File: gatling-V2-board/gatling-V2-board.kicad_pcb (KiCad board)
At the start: 2 copper layers, 65 x 45 mm, 33 parts, among them IC2 TRANSCEIVER_CAN_33, J1 645002114822, J10 61900311121, J11 61900311121, J12 61900311121, J13 61900311121, J2 62000411622, J3 61900311121, J4 61900311121, J5 691311700102, J7 653006114822, J9 62000411622, U1 Teensy3.2

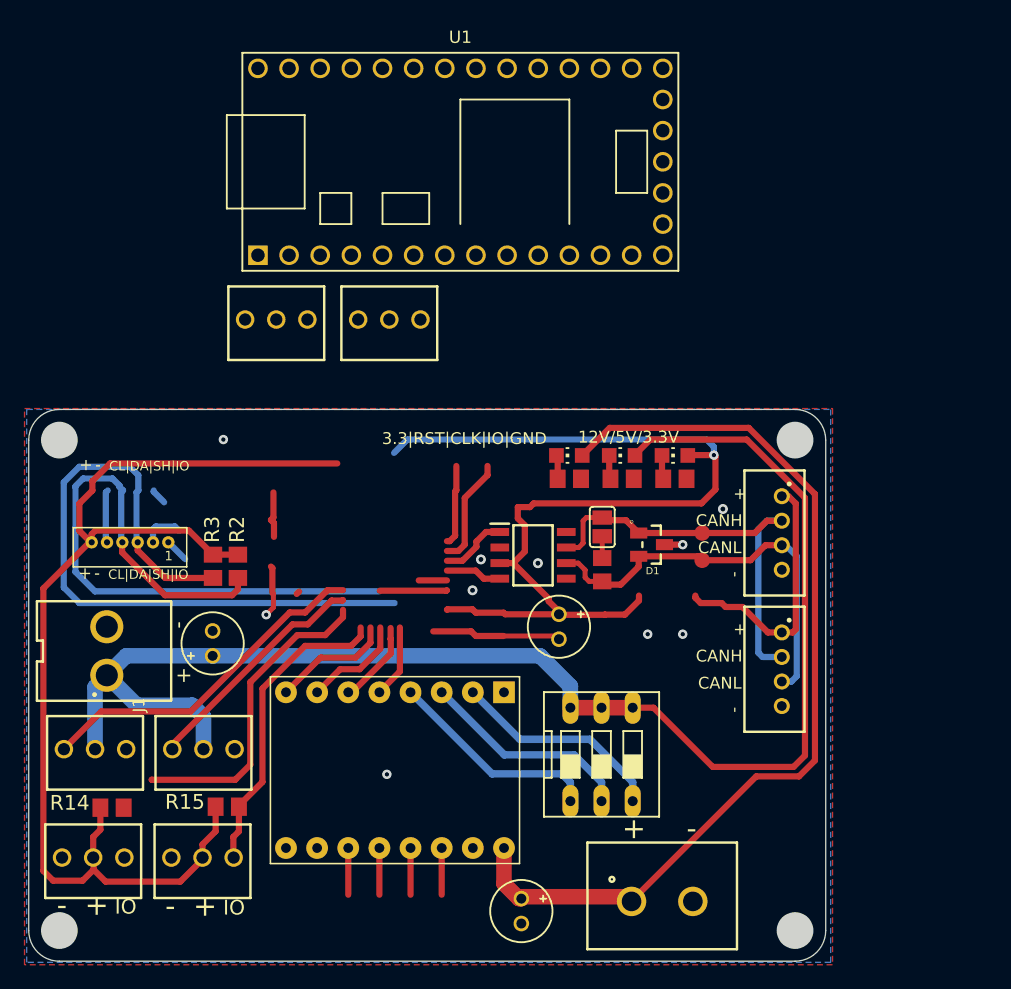
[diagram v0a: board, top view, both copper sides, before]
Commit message: Lib composant créée+pcb gatling mises à jours avec teensy (a verifier avant prod)
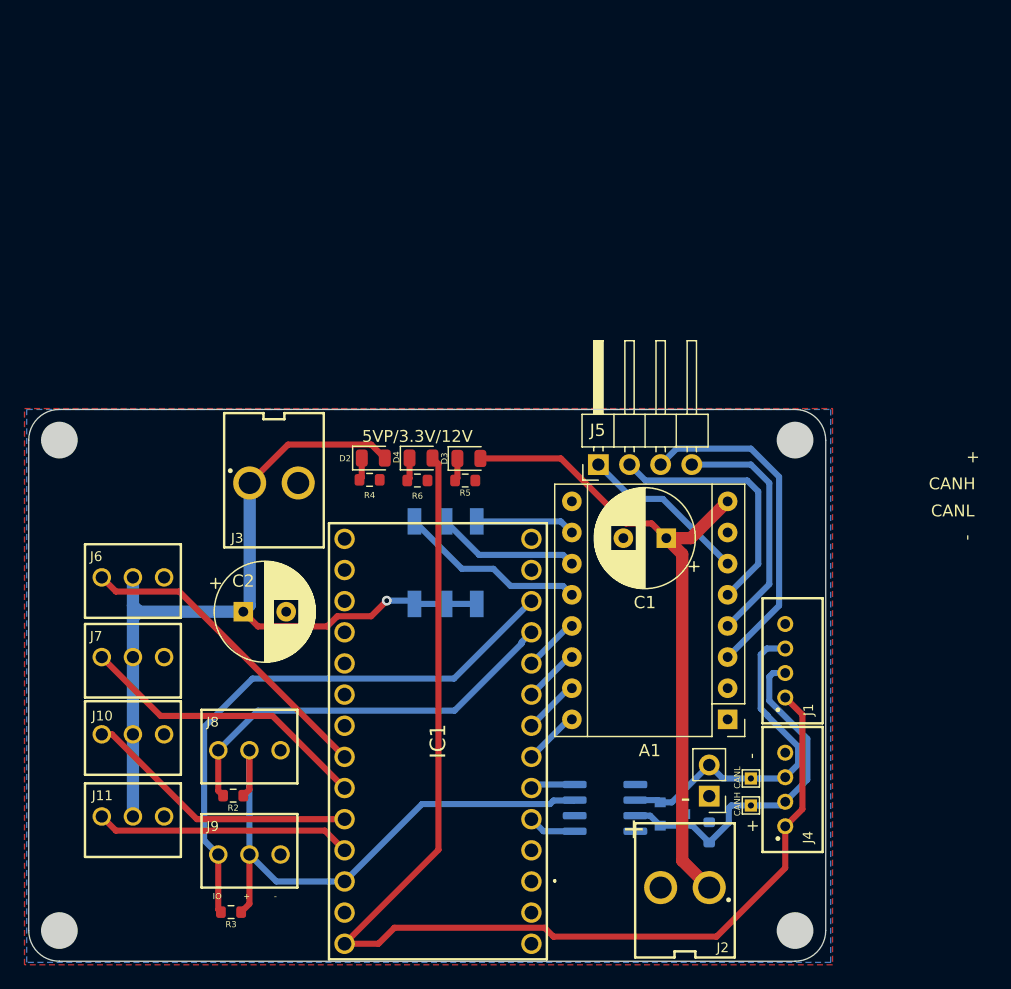
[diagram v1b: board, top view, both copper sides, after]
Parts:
- removed IC2: TRANSCEIVER_CAN_33, schematic prebarillet:SOIC127P600X175-8N
- removed J12, J13: 61900311121, schematic prebarillet:61900311121
- removed LED1, LED2, LED3: LED0805CHIP-LED0805, schematic prebarillet:CHIP-LED0805
- removed R12, R13: R0805R0805, schematic prebarillet:R0805
- removed R14, R15: R-EU_R0805, schematic prebarillet:R0805
- removed R7: 120, schematic prebarillet:R0805
- removed S1: DS03, schematic prebarillet:DS-03
- removed SJ1: SJ, schematic prebarillet:SJ
- removed U$1: DRV8825, schematic prebarillet:DRV8825
- removed U$2, U$3, U$4: 100uF, schematic prebarillet:E2-5
- added A1: Pololu_Breakout_DRV8825, Module:Pololu_Breakout-16_15.2x20.3mm, F.Cu at (173.0, 107.8)
- added C1: 100µF, Capacitor_THT:CP_Radial_D8.0mm_P3.50mm, F.Cu at (168.0, 93.0)
- added C2: 100µF, Capacitor_THT:CP_Radial_D8.0mm_P3.50mm, F.Cu at (133.5, 99.0)
- added D2: LED, LED_SMD:LED_0805_2012Metric, F.Cu at (144.1, 86.5)
- added D3: LED, LED_SMD:LED_0805_2012Metric, F.Cu at (151.9, 86.5)
- added D4: LED, LED_SMD:LED_0805_2012Metric, F.Cu at (148.0, 86.5)
- added IC1: TEENSY3.2, AREA_lib_composant:TEENSY32, F.Cu at (157.0, 121.0)
- added J6: Conn_01x03_Male, AREA_lib_Connector:Wuerth_2.54mm_3pins_61900311121, F.Cu at (124.5, 96.5)
- added J8: Conn_01x03_Male, AREA_lib_Connector:Wuerth_2.54mm_3pins_61900311121, F.Cu at (134.0, 110.0)
- added JP1: Jumper, Connector_PinHeader_2.54mm:PinHeader_1x02_P2.54mm_Vertical, F.Cu at (171.5, 114.0)
- added R4: 520, Resistor_SMD:R_0603_1608Metric, F.Cu at (143.8, 88.2)
- added R5: 520, Resistor_SMD:R_0603_1608Metric, F.Cu at (151.6, 88.3)
- added R6: 520, Resistor_SMD:R_0603_1608Metric, F.Cu at (147.7, 88.3)
- added SW1: SW_DIP_x03, Button_Switch_SMD:SW_DIP_SPSTx03_Slide_6.7x9.18mm_W6.73mm_P2.54mm_LowProfile_JPin, B.Cu at (150.0, 95.0)
- D1: value 5Vdc -> D_TVS_x2_AAC; footprint schematic prebarillet:WE-TVS_SOT23-3L -> Package_TO_SOT_SMD:SOT-23; moved to B.Cu
- J1: value 645002114822 -> Conn_01x04_Male; footprint schematic prebarillet:645002114822 -> AREA_lib_Connector:Wuerth_2mm_4pin_62000411622
- J10, J11: value 61900311121 -> Conn_01x03_Male; footprint schematic prebarillet:61900311121 -> AREA_lib_Connector:Wuerth_2.54mm_3pins_61900311121
- J2: value 62000411622 -> Conn_01x02_Male; footprint schematic prebarillet:62000411622 -> AREA_lib_Connector:Wuerth_3.96mm_2pin_645002114822
- J3: value 61900311121 -> Conn_01x02_Male; footprint schematic prebarillet:61900311121 -> AREA_lib_Connector:Wuerth_3.96mm_2pin_645002114822
- J4: value 61900311121 -> Conn_01x04_Male; footprint schematic prebarillet:61900311121 -> AREA_lib_Connector:Wuerth_2mm_4pin_62000411622
- J5: value 691311700102 -> Conn_01x04_Male; footprint schematic prebarillet:691311700102 -> Connector_PinHeader_2.54mm:PinHeader_1x04_P2.54mm_Horizontal
- J7: value 653006114822 -> Conn_01x03_Male; footprint schematic prebarillet:653006114822 -> AREA_lib_Connector:Wuerth_2.54mm_3pins_61900311121
- J9: value 62000411622 -> Conn_01x03_Male; footprint schematic prebarillet:62000411622 -> AREA_lib_Connector:Wuerth_2.54mm_3pins_61900311121
- R1: value R0805R0805 -> 120; footprint schematic prebarillet:R0805 -> Resistor_SMD:R_0603_1608Metric; moved to B.Cu
- R2, R3: value R-EU_R0805 -> 10K; footprint schematic prebarillet:R0805 -> Resistor_SMD:R_0603_1608Metric
- TP1, TP2: value TEST-POINT3X5 -> TestPoint; footprint schematic prebarillet:PAD.03X.05 -> TestPoint:TestPoint_THTPad_1.0x1.0mm_Drill0.5mm
- U1: value Teensy3.2 -> SN65HVD232; footprint teensy:Teensy30_31_32_LC -> Package_SO:SOIC-8_3.9x4.9mm_P1.27mm; moved to B.Cu
- moved J1 56.4 mm to (178.3, 103.0)
- moved U1 54.0 mm to (163.0, 115.0)
- moved J4 50.3 mm to (178.3, 113.5), turned to 270 degrees
- moved J9 45.3 mm to (134.0, 118.5), turned to 180 degrees
- moved J5 36.0 mm to (162.5, 87.0), turned to 90 degrees
- moved R1 31.0 mm to (171.5, 117.0), turned to 270 degrees
- moved J2 30.3 mm to (169.5, 122.0), turned to 0 degrees
- moved R3 28.2 mm to (132.5, 123.5), turned to 180 degrees
- moved TP1 22.6 mm to (174.9, 114.8), turned to 90 degrees
- moved D1 22.0 mm to (168.5, 115.5), turned to 0 degrees
- moved R2 18.7 mm to (132.7, 114.0), turned to 180 degrees
- moved TP2 18.2 mm to (174.9, 112.6), turned to 90 degrees
- moved J3 12.5 mm to (136.0, 88.0), turned to 180 degrees
- moved J7 9.66 mm to (124.5, 103.0)
- moved J11 7.95 mm to (124.5, 116.0)
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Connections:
- D1 pad 1: /CANH -> CANH
- D1 pad 2: /CANL -> CANL
- J1 pad 2: GND -> CANH
- J10 pad 2: +5V -> +5VP
- J10 pad 3: /SERVO1 -> SERVO3
- J11 pad 2: +5V -> +5VP
- J11 pad 3: /SERVO2 -> SERVO4
- J2 pad 1: /5VC -> +12V
- J2 pad 2: /CANH -> GND
- J3 pad 1: GND -> +5VP
- J3 pad 2: +5V -> GND
- J4 pad 1: GND -> +5V
- J4 pad 2: +5V -> CANH
- J4 pad 3: /SERVO4 -> CANL
- J5 pad 1: /+12V -> Net-(A1-Pad6)
- J5 pad 2: GND -> Net-(A1-Pad5)
- J7 pad 1: /GPIO1 -> GND
- J7 pad 2: /XSHUT1 -> +5VP
- J7 pad 3: /SDA -> SERVO2
- J9 pad 1: /5VC -> FOURCHE2
- J9 pad 2: /CANH -> +3V3
- J9 pad 3: /CANL -> GND
- R1 pad 1: GND -> Net-(JP1-Pad1)
- R1 pad 2: Net-(LED3-PadC) -> CANH
- R2 pad 1: /SCL -> +3V3
- R2 pad 2: /+3.3V -> FOURCHE1
- R3 pad 1: /SDA -> +3V3
- R3 pad 2: /+3.3V -> FOURCHE2
- U1 pad 1: GND -> CAN_TX
- U1 pad 2: Net-(U1-Pad2) -> GND
- U1 pad 3: Net-(U1-Pad3) -> +3V3
- U1 pad 4: /DIR -> CAN_RX
- U1 pad 5: /CANTX -> (no net)
- U1 pad 6: /CANRX -> CANL
- U1 pad 7: /SLIP -> CANH
- U1 pad 8: /STEP -> (no net)
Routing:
- net /+3.3V: track 171.4 -> 0.00 mm, vias 1 -> 0
- net /+12V: track 77.7 -> 0.00 mm
- net +5VP: track 0.00 -> 73.4 mm, vias 0 -> 1
- net /SCL: track 59.7 -> 0.00 mm
- net /SDA: track 58.8 -> 0.00 mm
- net +12V: track 0.00 -> 54.0 mm
- net +3V3: track 0.00 -> 47.6 mm
- net FOURCHE2: track 0.00 -> 46.6 mm
- net /CANH: track 34.9 -> 0.00 mm
- net /CANL: track 33.5 -> 0.00 mm
- net FOURCHE1: track 0.00 -> 33.5 mm
- net CANH: track 0.00 -> 28.9 mm
- net /SERVO1: track 28.1 -> 0.00 mm
- net CANL: track 0.00 -> 28.0 mm
- net Net-(A1-Pad3): track 0.00 -> 27.6 mm
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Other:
- net class Default: clearance 0.2 -> 0.15
- rule trace_clearance: 0.2 -> 0.15
- board text added: "5VP/3.3V/12V"
- board text added: "Carte pre-barillet /*A.R.E.A.OLD*/ V2 PA-github.com/kingovchouffe"
- board text removed: "12V/5V/3.3V"
- board text removed: "3.3|RST|CLK|IO|GND"
- board text removed: "CL|DA|SH|IO"
- board text removed: "Carte pre-barillet /*A.R.E.A.OLD*/ V1 PA-github.com/kingovchouffe"

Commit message: prete pour inspection
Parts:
- SW1: moved to F.Cu
- moved C1 0.40 mm to (168.4, 93.0)
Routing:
- net Net-(A1-Pad10): track 8.13 -> 15.8 mm, vias 0 -> 1
- net +5V: track 97.1 -> 103.4 mm
- net Net-(A1-Pad12): track 15.3 -> 12.4 mm, vias 0 -> 1
- net Net-(A1-Pad11): track 11.7 -> 12.8 mm, vias 0 -> 1
- net SERVO3: track 22.7 -> 23.3 mm
- net +5VP: track 73.4 -> 73.7 mm, vias 1 -> 0
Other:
- board text added: "12V"
- board text added: "5V"
- board text added: "SERVO1"
- board text added: "SERVO2"
- board text added: "SERVO3"
- board text added: "SERVO4"

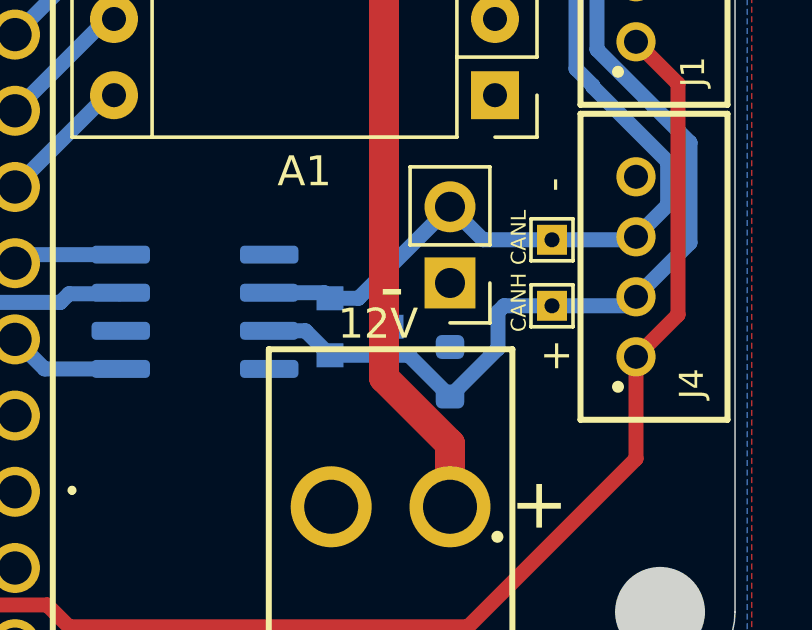
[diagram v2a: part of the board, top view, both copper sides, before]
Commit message: connect wire that weren't connected
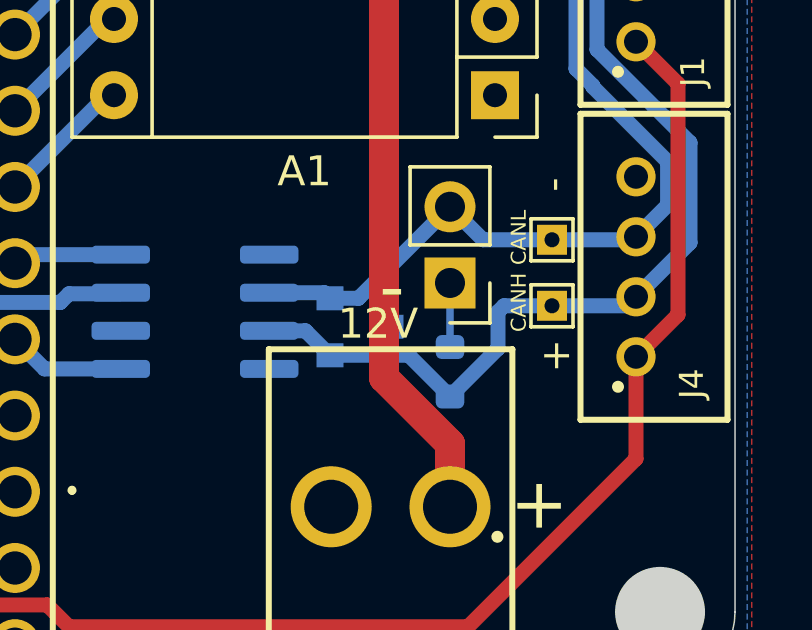
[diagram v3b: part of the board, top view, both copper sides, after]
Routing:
- net Net-(JP1-Pad1): track 0.00 -> 2.13 mm
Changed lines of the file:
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@@
-(kicad_pcb (version 20171130) (host pcbnew "(5.1.8)-1")
+(kicad_pcb (version 20171130) (host pcbnew "(5.1.6)-1")
   (general
     (thickness 1.6)
     (drawings 35)
-    (tracks 182)
+    (tracks 183)
     (zones 0)
     (modules 30)
@@
   )
   (setup
-    (last_trace_width 0.5)
+    (last_trace_width 0.25)
     (user_trace_width 0.5)
     (user_trace_width 0.75)
@@
   (segment (start 157.985 116.905) (end 160.525 116.905) (width 0.5) (layer B.Cu) (net 29))
   (segment (start 157 115.92) (end 157.985 116.905) (width 0.5) (layer B.Cu) (net 29))
+  (segment (start 171.5 116.175) (end 171.5 114.04) (width 0.25) (layer B.Cu) (net 30))
   (zone (net 1) (net_name GND) (layer B.Cu) (hatch edge 0.508)
     (priority 6)
     (connect_pads (clearance 0.000001))
     (min_thickness 0.0762)
-    (fill (arc_segments 32) (thermal_gap 0.2024) (thermal_bridge_width 0.2024))
+    (fill yes (arc_segments 32) (thermal_gap 0.2024) (thermal_bridge_width 0.2024))
     (polygon
       (pts
@@
     (connect_pads (clearance 0.000001))
     (min_thickness 0.2032)
-    (fill (arc_segments 32) (thermal_gap 0.4564) (thermal_bridge_width 0.4564))
+    (fill yes (arc_segments 32) (thermal_gap 0.4564) (thermal_bridge_width 0.4564))
     (polygon
       (pts

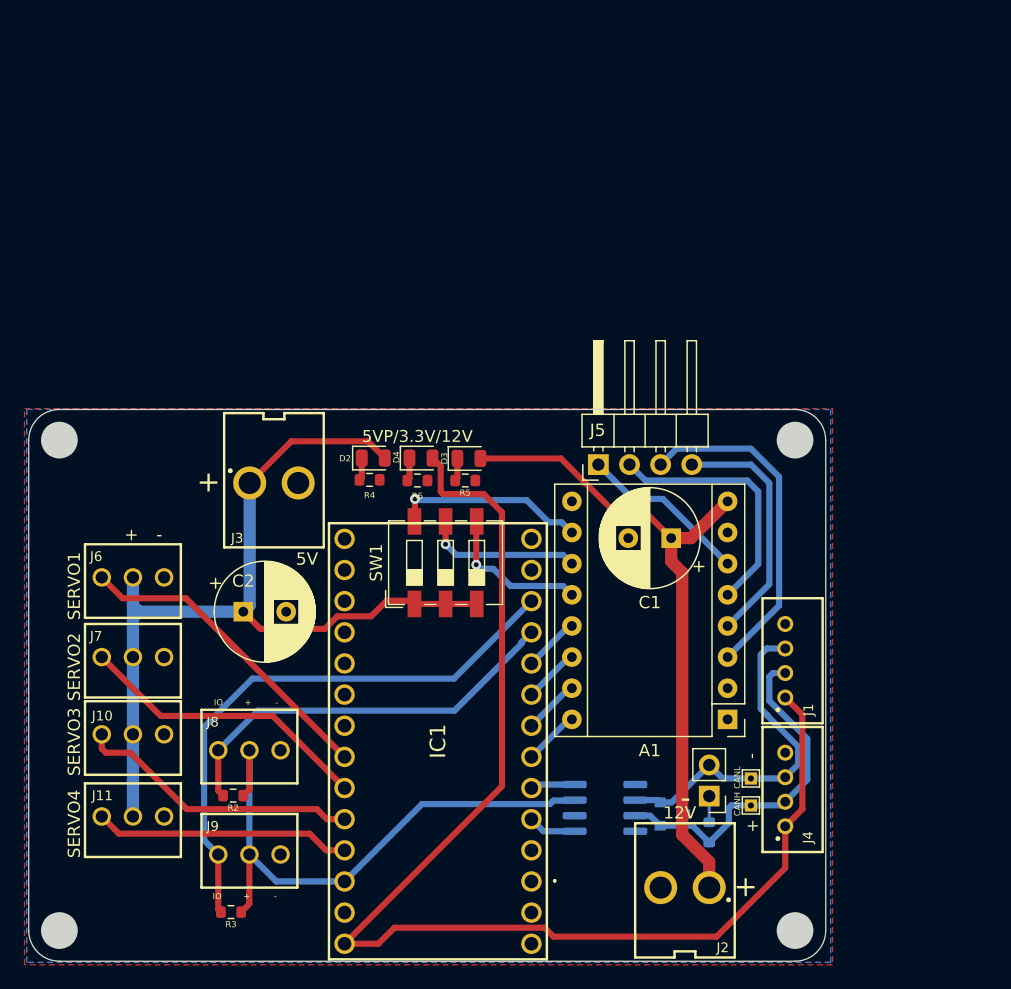
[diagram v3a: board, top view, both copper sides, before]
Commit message: moving some traces
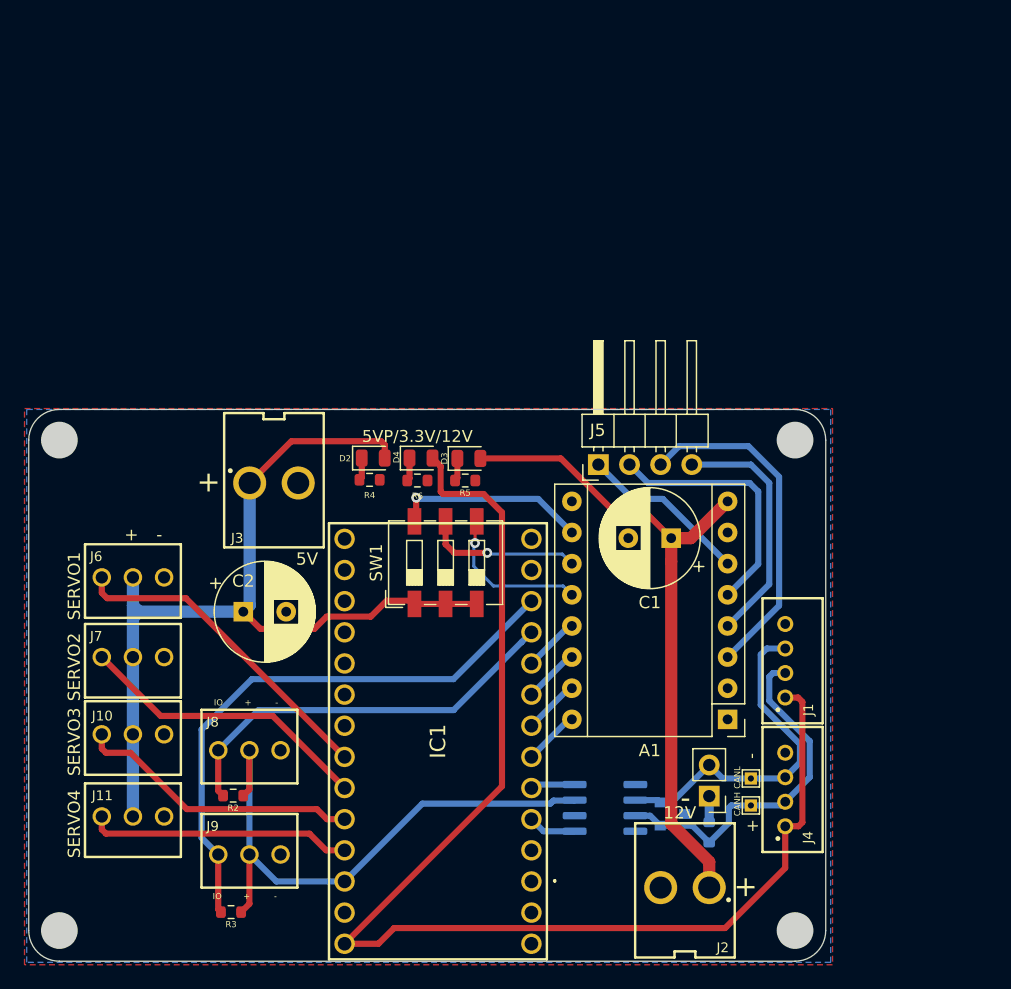
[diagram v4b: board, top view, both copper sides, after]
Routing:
- net SERVO1: track 25.9 -> 26.6 mm
- net +5V: track 103.4 -> 104.0 mm
- net +5VP: track 73.7 -> 74.4 mm
- net SERVO4: track 20.9 -> 21.6 mm

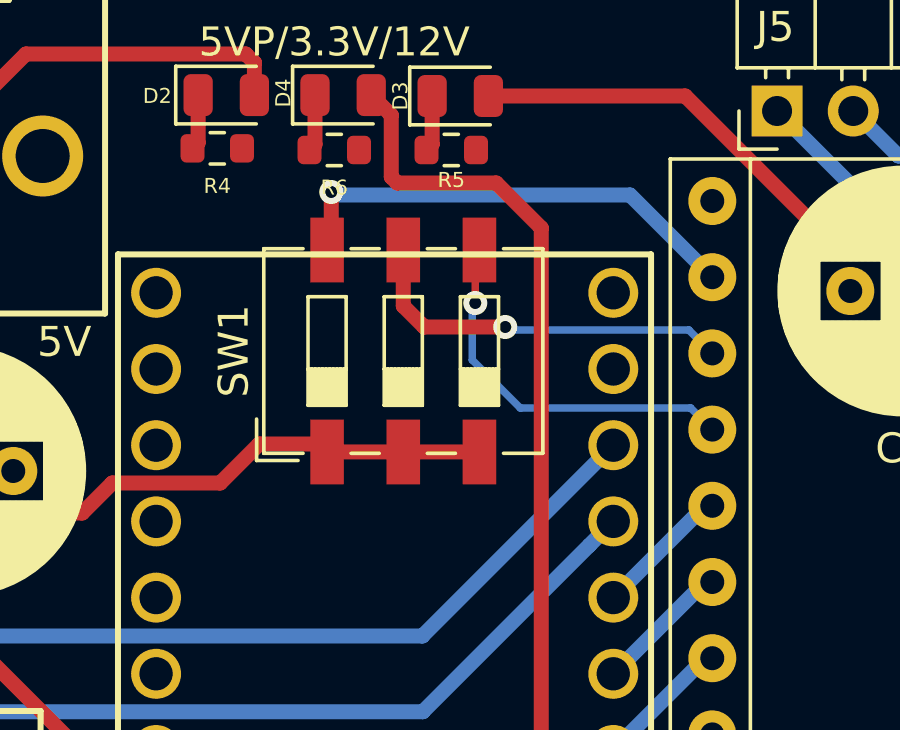
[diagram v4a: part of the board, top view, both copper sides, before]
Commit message: Change dip switch for wurth dip sw
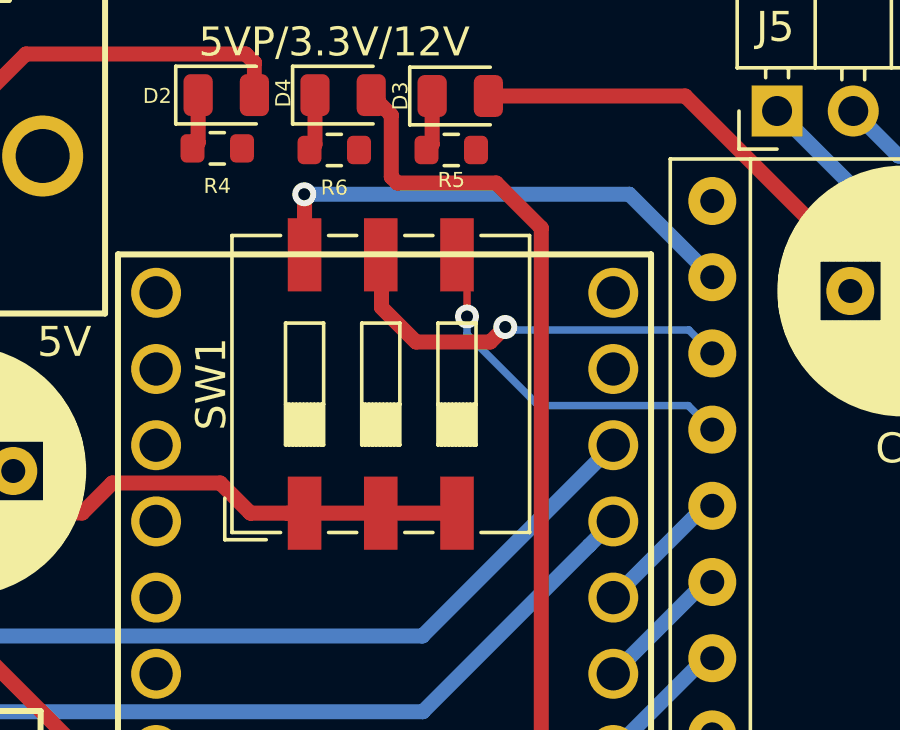
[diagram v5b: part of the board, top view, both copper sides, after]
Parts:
- SW1: footprint Button_Switch_SMD:SW_DIP_SPSTx03_Slide_6.7x9.18mm_W6.73mm_P2.54mm_LowProfile_JPin -> Button_Switch_SMD:SW_DIP_SPSTx03_Slide_9.78x9.8mm_W8.61mm_P2.54mm
- moved SW1 1.33 mm to (149.2, 96.1)
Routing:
- net Net-(A1-Pad11): track 12.8 -> 13.8 mm
- net +5VP: track 74.4 -> 73.5 mm
- net Net-(A1-Pad10): track 15.9 -> 16.8 mm
